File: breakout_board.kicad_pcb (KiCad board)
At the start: 2 copper layers, 55.2 x 66.7 mm, 19 parts, among them J1 PJ-102A, J2 Conn_01x09_Male, J3 Conn_01x09_Male, J4 Conn_01x10_Male, J5 Conn_01x08_Male, J6 Conn_01x09_Male, J7 Conn_01x10_Male, J8 Conn_01x02_Male, J9 AVR-ISP-6, U1 ATmega1281-16AU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

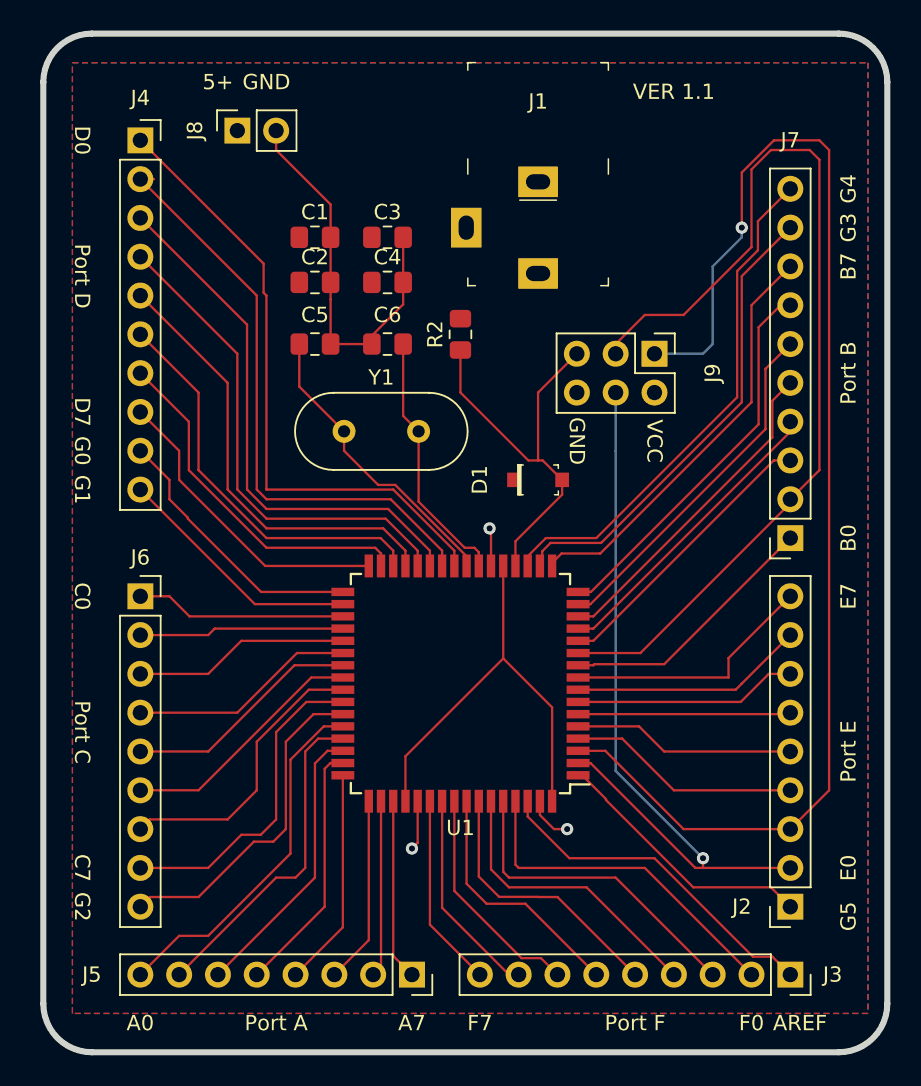
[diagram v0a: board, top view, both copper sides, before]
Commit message: Add files via upload
Fixed incorrect silkscreen pin labels, added silkscreen labels for pin functionality. Added reset button to reset the microcontroller
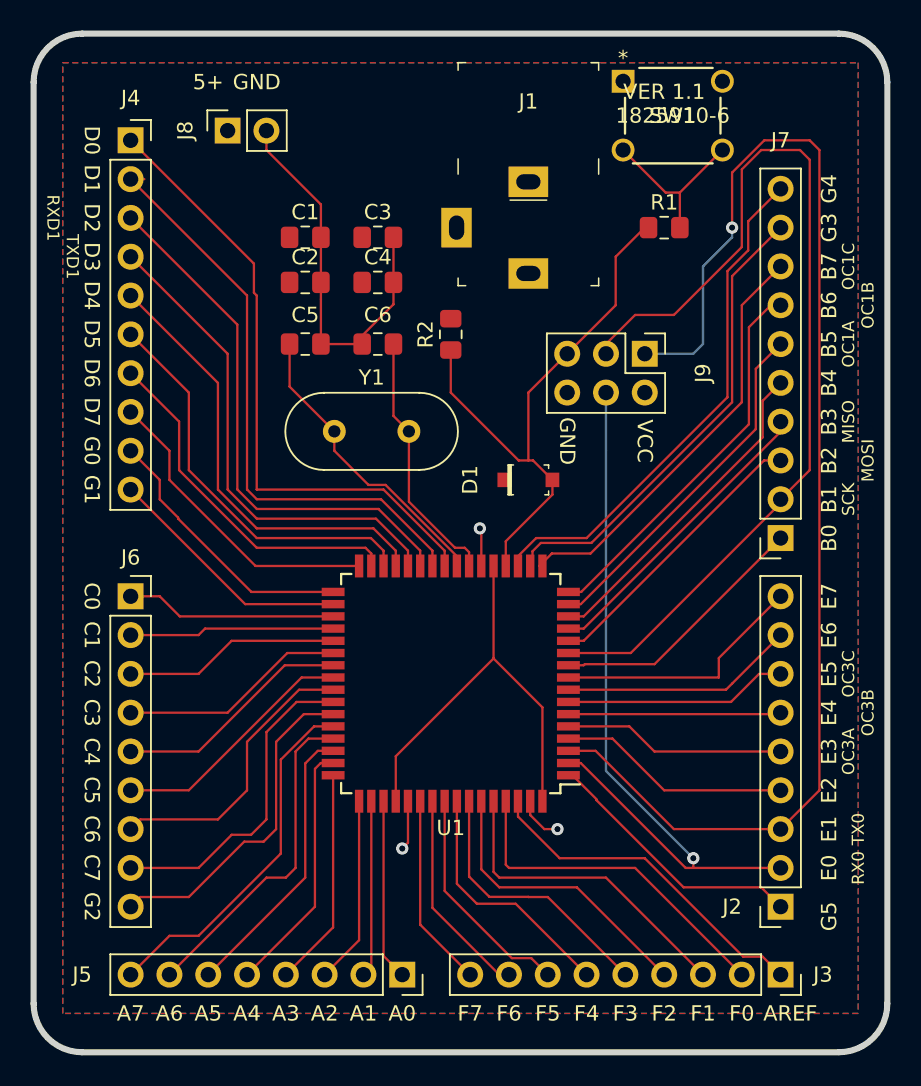
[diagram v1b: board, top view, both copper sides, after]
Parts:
- added R1: 330, Resistor_SMD:R_0805_2012Metric_Pad1.15x1.40mm_HandSolder, F.Cu at (151.1, 45.7)
- added SW1: 1825910-6, footprints:1825910-6, F.Cu at (154.9, 40.6)
- moved C3 0.64 mm to (132.4, 46.4)
- moved C4 0.64 mm to (132.4, 49.3)
- moved C6 0.64 mm to (132.4, 53.3)
- moved Y1 0.64 mm to (129.5, 59.1)
- moved C1 0.64 mm to (127.6, 46.4)
- moved C2 0.64 mm to (127.6, 49.3)
- moved C5 0.64 mm to (127.6, 53.3)
- moved J4 0.64 mm to (116.2, 40.0)
- moved J6 0.64 mm to (116.2, 69.8)
- moved D1 0.63 mm to (142.2, 62.2)
- moved J1 0.63 mm to (142.2, 45.7)
- moved J2 0.63 mm to (158.8, 90.2)
- moved J3 0.63 mm to (158.8, 94.6)
- moved J5 0.63 mm to (134.0, 94.6)
- moved J7 0.63 mm to (158.8, 66.0)
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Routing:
- net Net-(R1-Pad2): track 0.00 -> 11.1 mm
- net Reset: track 27.0 -> 37.7 mm
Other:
- board size 55.2 x 66.7 mm -> 55.9 x 66.7 mm
- board text added: "A1"
- board text added: "A2"
- board text added: "A3"
- board text added: "A4"
- board text added: "A5"
- board text added: "A6"
- board text added: "B1"
- board text added: "B2"
- board text added: "B3"
- board text added: "B4"
- board text added: "B5"
- board text added: "B6"
- board text added: "C1"
- board text added: "C2"
- board text added: "C3"
- board text added: "C4"
- board text added: "C5"
- board text added: "C6"
- board text added: "D1"
- board text added: "D2"
- board text added: "D3"
- board text added: "D4"
- board text added: "D5"
- board text added: "D6"
- board text added: "E1"
- board text added: "E2"
- board text added: "E3"
- board text added: "E4"
- board text added: "E5"
- board text added: "E6"
- board text added: "F1"
- board text added: "F2"
- board text added: "F3"
- board text added: "F4"
- board text added: "F5"
- board text added: "F6"
- board text added: "MISO"
- board text added: "MOSI"
- board text added: "OC1A"
- board text added: "OC1B"
- board text added: "OC1C"
- board text added: "OC3A"
- board text added: "OC3B"
- board text added: "OC3C"
- board text added: "RX0"
- board text added: "RXD1"
- board text added: "SCK"
- board text added: "TX0"
- board text added: "TXD1"
- board text removed: "Port A"
- board text removed: "Port B"
- board text removed: "Port C"
- board text removed: "Port D"
- board text removed: "Port E"
- board text removed: "Port F"
